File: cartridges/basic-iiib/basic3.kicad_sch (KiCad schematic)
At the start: 9 parts, among them SW1 SW_SPDT, U1 27C512, U2 SG-1000-Cart, U3 UM61512

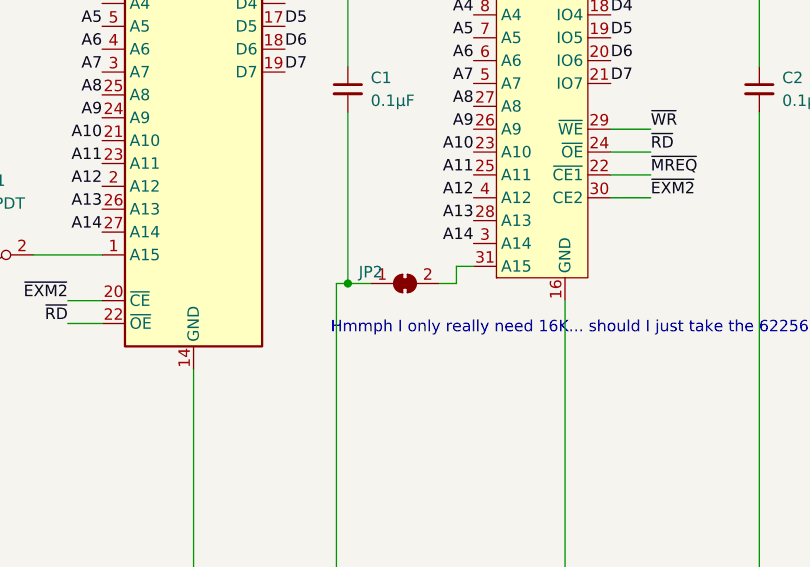
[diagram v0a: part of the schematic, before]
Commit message: Carts to KiCad 7
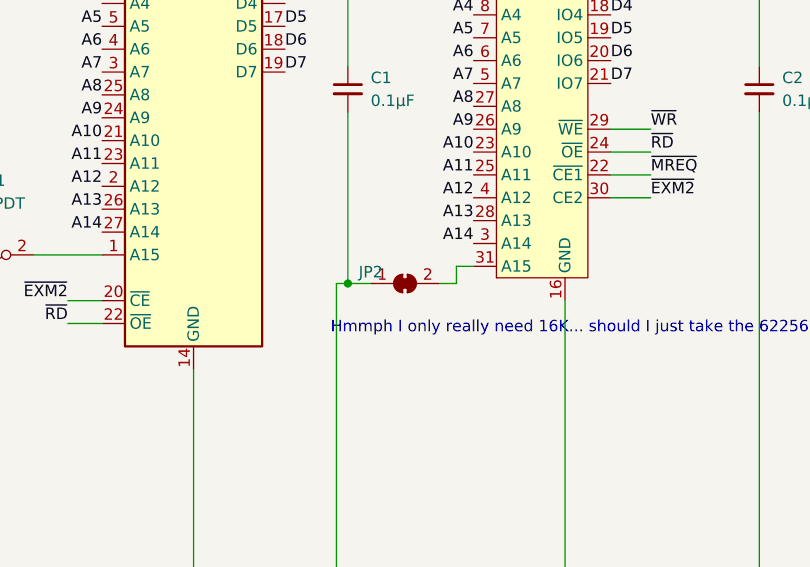
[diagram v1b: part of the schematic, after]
